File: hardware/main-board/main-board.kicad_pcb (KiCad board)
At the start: 2 copper layers, 180 x 55 mm, 96 parts, among them J1 BARREL_JACK, J2 CONN_01X10, J3 CONN_01X10, J4 USB_OTG, J5 CONN_02X05, J6 SMA, Q1 DDTD113ZC, Q2 DDTD113ZC, Q3 DDTD113ZC, Q4 DDTD113ZC, Q5 DDTD113ZC, Q6 FDB14N30TM, Q7 DDTD113ZC, Q8 DDTD113ZC, Q9 DDTD113ZC, SW1 SW_Push, SW2 SW_Push, SW3 SW_Push, SW4 SW_Push, U1 LD1117S33TR, U2 MAX1771, U3 STM32F302C, U4 FGPMMOPA6H, Y1 8MHz, Y2 32.768kHz

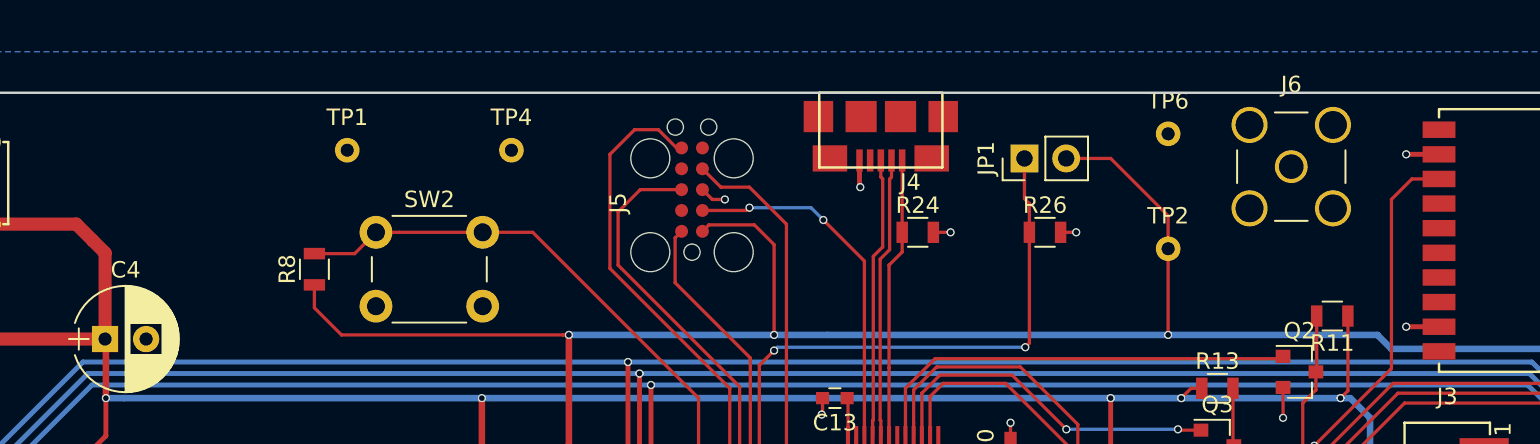
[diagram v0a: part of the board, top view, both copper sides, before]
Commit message: Working on main board layout
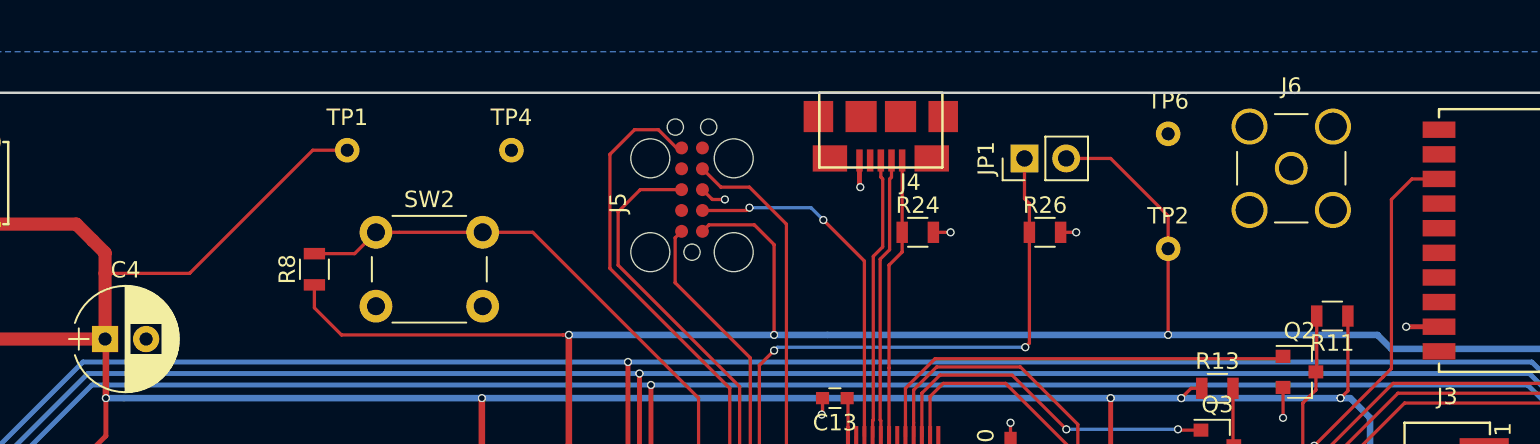
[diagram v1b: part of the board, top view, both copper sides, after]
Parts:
- moved J6 0.10 mm to (202.5, 67.1)
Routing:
- net +12V: track 323.1 -> 340.9 mm
- net GND: track 90.2 -> 88.2 mm, vias 56 -> 55
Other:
- rule trace_min: 0.2 -> 0.16
- rule via_min_drill: 0.34 -> 0.3
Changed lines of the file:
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@@
   (general
     (links 231)
-    (no_connects 14)
+    (no_connects 7)
     (area 59.924999 62.424999 240.075001 117.575001)
     (thickness 1.6)
     (drawings 28)
-    (tracks 898)
+    (tracks 900)
     (zones 0)
     (modules 96)
@@
   )
   (setup
-    (last_trace_width 0.3)
+    (last_trace_width 0.2)
     (user_trace_width 0.3)
     (user_trace_width 0.4)
@@
     (zone_clearance 0.5)
     (zone_45_only no)
-    (trace_min 0.2)
+    (trace_min 0.16)
     (segment_width 0.15)
     (edge_width 0.15)
@@
     (via_drill 0.34)
     (via_min_size 0.5)
-    (via_min_drill 0.34)
+    (via_min_drill 0.3)
     (user_via 0.7 0.5)
     (uvia_size 0.5)
@@
     (uvias_allowed no)
     (uvia_min_size 0.5)
-    (uvia_min_drill 0.34)
+    (uvia_min_drill 0.3)
     (pcb_text_width 0.3)
     (pcb_text_size 1.5 1.5)
@@
   )
   (module Connect:SMA_THT_Jack_Straight (layer F.Cu)
-    (at 202.5 67)
+    (at 202.5 67.1)
     (descr "SMA pcb through hole jack")
     (tags "SMA THT Jack Straight")
@@
       (effects (font (size 1 1) (thickness 0.15)))
     )
-    (fp_text value MountingHole_3.2mm_M3_Pad (at 0 4.2) (layer F.Fab)
+    (fp_text value MountingHole_3.2mm_M3_Pad (at 0 4.2) (layer F.Fab) hide
       (effects (font (size 1 1) (thickness 0.15)))
     )
@@
       (effects (font (size 1 1) (thickness 0.15)))
     )
-    (fp_text value MountingHole_3.2mm_M3_Pad (at 0 4.2) (layer F.Fab)
+    (fp_text value MountingHole_3.2mm_M3_Pad (at 0 4.2) (layer F.Fab) hide
       (effects (font (size 1 1) (thickness 0.15)))
     )
@@
       (effects (font (size 1 1) (thickness 0.15)))
     )
-    (fp_text value MountingHole_3.2mm_M3_Pad (at 0 4.2) (layer F.Fab)
+    (fp_text value MountingHole_3.2mm_M3_Pad (at 0 4.2) (layer F.Fab) hide
       (effects (font (size 1 1) (thickness 0.15)))
     )
@@
       (effects (font (size 1 1) (thickness 0.15)))
     )
-    (fp_text value MountingHole_3.2mm_M3_Pad (at 0 4.2) (layer F.Fab)
+    (fp_text value MountingHole_3.2mm_M3_Pad (at 0 4.2) (layer F.Fab) hide
       (effects (font (size 1 1) (thickness 0.15)))
     )
@@
   (segment (start 83.305 85.555) (end 83.25 85.5) (width 0.6) (layer F.Cu) (net 1))
   (via (at 83.25 85.5) (size 0.7) (drill 0.5) (layers F.Cu B.Cu) (net 1))
-  (segment (start 211.5 66.25) (end 209.5 66.25) (width 0.3) (layer F.Cu) (net 1))
-  (via (at 209.5 66.25) (size 0.5) (drill 0.34) (layers F.Cu B.Cu) (net 1))
   (segment (start 211.5 76.75) (end 209.5 76.75) (width 0.3) (layer F.Cu) (net 1))
   (via (at 209.5 76.75) (size 0.5) (drill 0.34) (layers F.Cu B.Cu) (net 1))
@@
   (via (at 174.6 96) (size 0.5) (drill 0.34) (layers F.Cu B.Cu) (net 2))
   (segment (start 206.5 107.5) (end 211.8 107.5) (width 0.2) (layer F.Cu) (net 2))
+  (segment (start 145 66) (end 142.9 66) (width 0.2) (layer F.Cu) (net 3))
+  (segment (start 142.9 66) (end 135.4 73.5) (width 0.2) (layer F.Cu) (net 3))
+  (segment (start 135.4 73.5) (end 130.25 73.5) (width 0.2) (layer F.Cu) (net 3))
+  (segment (start 130.25 77.5) (end 130.25 73.5) (width 0.8) (layer F.Cu) (net 3))
+  (segment (start 130.25 73.5) (end 130.25 72.25) (width 0.8) (layer F.Cu) (net 3))
   (segment (start 67.55 90) (end 67.55 93) (width 0.3) (layer F.Cu) (net 3))
   (segment (start 67.55 87) (end 67.55 90) (width 0.3) (layer F.Cu) (net 3))
@@
   (via (at 65.75 87) (size 0.7) (drill 0.5) (layers F.Cu B.Cu) (net 3))
   (segment (start 119.5 77.5) (end 130.25 77.5) (width 0.8) (layer F.Cu) (net 3))
-  (segment (start 130.25 77.5) (end 130.25 72.25) (width 0.8) (layer F.Cu) (net 3))
   (segment (start 128.5 70.5) (end 123.1 70.5) (width 0.8) (layer F.Cu) (net 3))
   (segment (start 123.1 65.5) (end 123.1 70.5) (width 0.8) (layer F.Cu) (net 3))

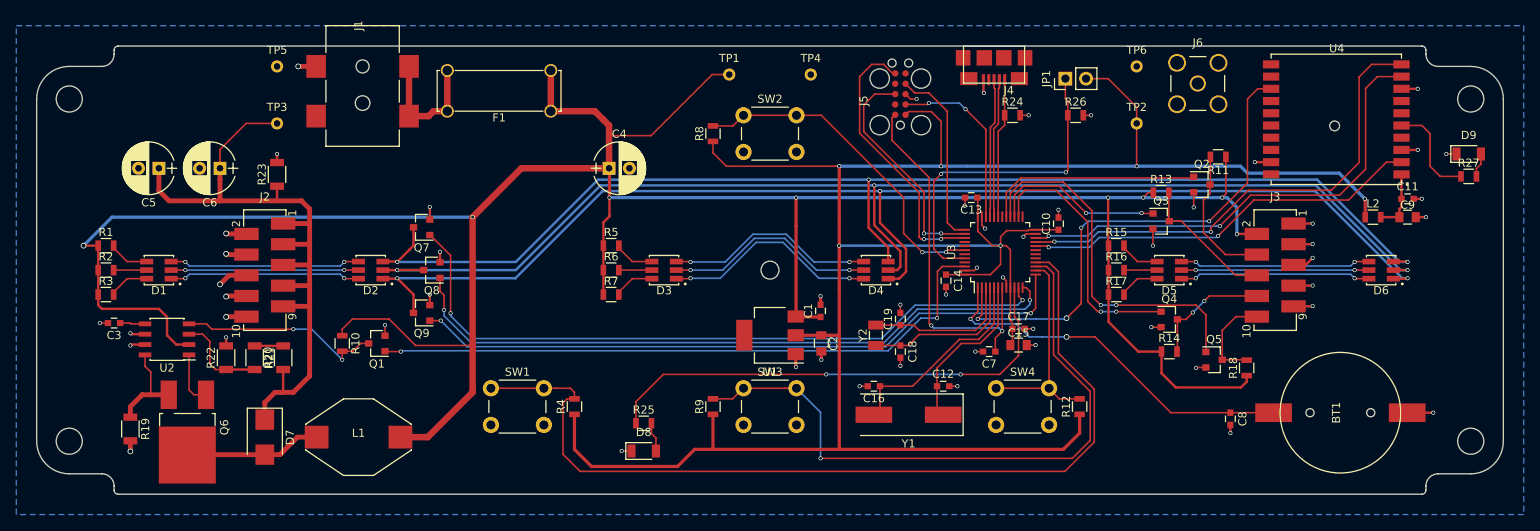
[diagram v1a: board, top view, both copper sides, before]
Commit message: Working on main board layout
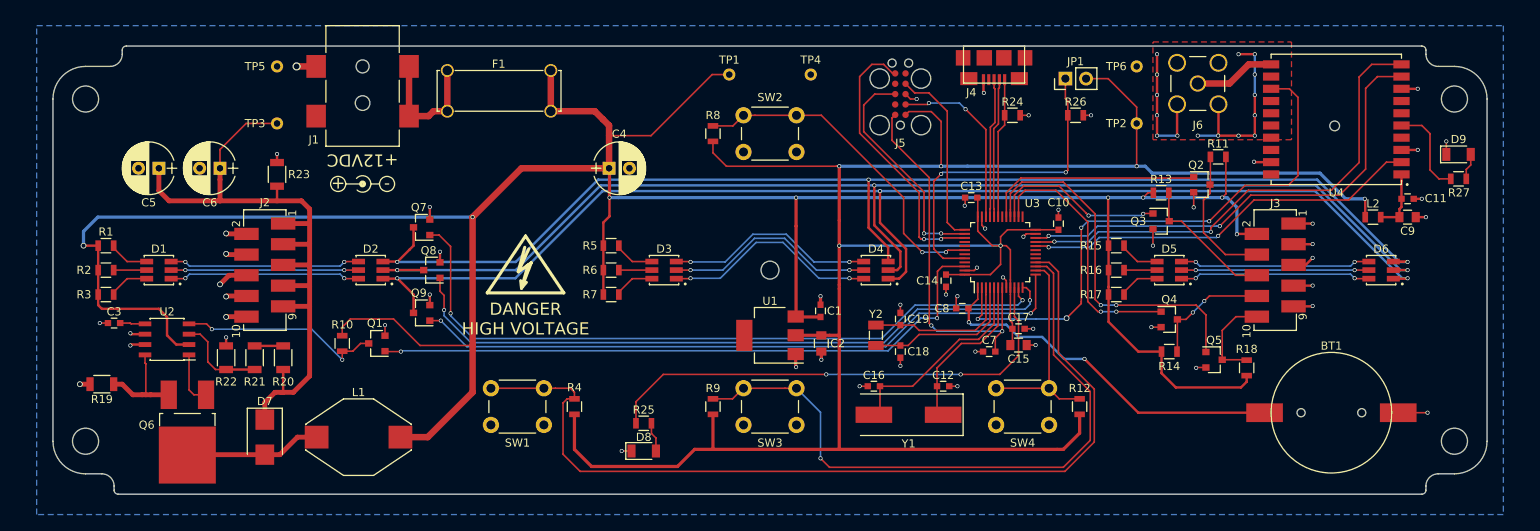
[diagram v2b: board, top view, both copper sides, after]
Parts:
- added REF**: Symbol_HighVoltage_Type2_CopperTop_VerySmall, radio-clock:Symbol_HighVoltage_Type2_SilkscreenTop_VerySmall, F.Cu at (120.0, 90.0)
- added REF**: Symbol_Barrel_Polarity, Symbols:Symbol_Barrel_Polarity, F.Cu at (100.0, 79.5)
- moved C8 35.6 mm to (173.6, 94.7), turned to 180 degrees
- moved R19 6.52 mm to (68.0, 104.0), turned to 180 degrees
- moved REF** 2.00 mm to (66.0, 69.0)
- moved REF** 2.00 mm to (66.0, 111.0)
- moved REF** 2.00 mm to (234.0, 69.0)
- moved REF** 2.00 mm to (234.0, 111.0)
- moved R27 1.29 mm to (234.5, 78.8)
- moved D9 1.25 mm to (234.5, 75.8)
- moved BT1 1.10 mm to (218.9, 107.5)
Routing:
- net GND: track 88.2 -> 129.0 mm, vias 55 -> 70
- net Net-(J6-Pad1): track 0.00 -> 9.97 mm
- net /GPS_PPS: track 63.2 -> 69.4 mm
- net +12V: track 340.9 -> 342.1 mm
- net /PB2: track 79.5 -> 80.4 mm
- net Net-(R27-Pad1): track 12.2 -> 11.4 mm
- net /LED_RED: track 86.0 -> 86.7 mm
- net Net-(BT1-Pad1): track 46.2 -> 45.7 mm
- added copper zone on F.Cu, net GND
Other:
- board size 180 x 55 mm -> 176 x 55 mm
- board text added: "+"
- board text added: "+12VDC"
- board text added: "-"
- board text added: "DANGER HIGH VOLTAGE"

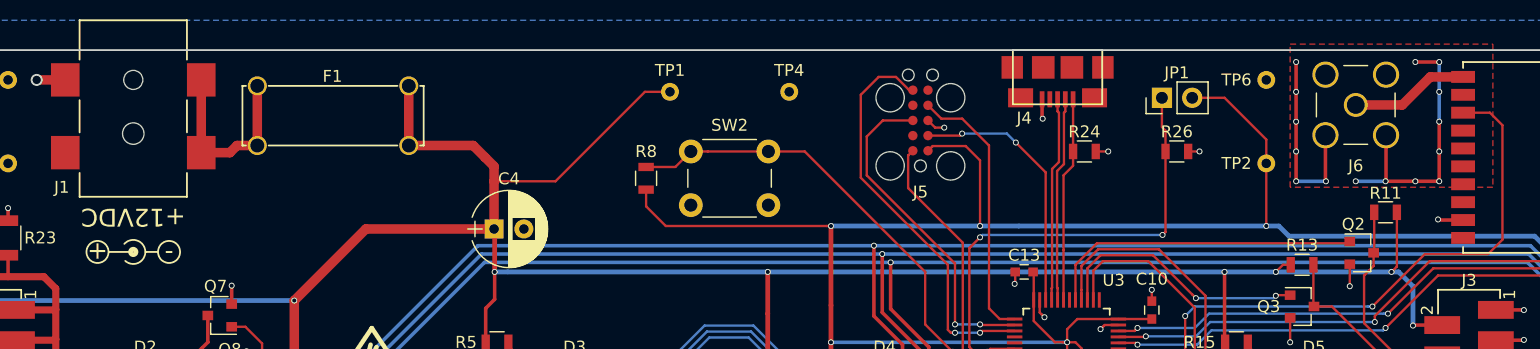
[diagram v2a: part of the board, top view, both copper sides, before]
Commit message: Working on main board layout
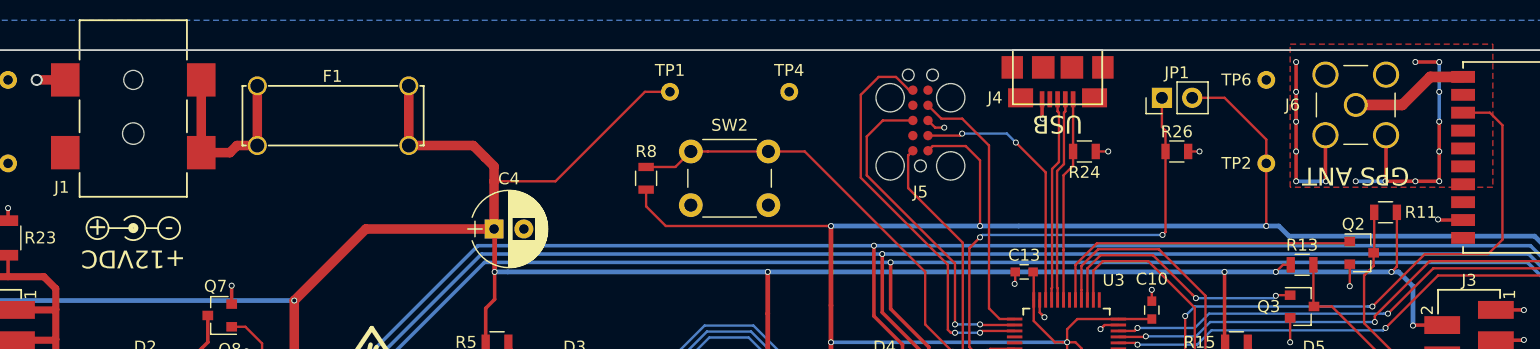
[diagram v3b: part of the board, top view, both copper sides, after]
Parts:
- moved REF** 2.00 mm to (100.0, 77.5)
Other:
- board text added: "GPS ANT"
- board text added: "USB"
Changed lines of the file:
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@@
     (area 61.924999 62.424999 238.075001 117.575001)
     (thickness 1.6)
-    (drawings 32)
+    (drawings 34)
     (tracks 942)
     (zones 0)
@@
   (module radio-clock:10118192 (layer F.Cu)
     (at 177.5 62.5 180)
-    (fp_text reference J4 (at 2.8 -5.7 180) (layer F.SilkS)
+    (fp_text reference J4 (at 5.25 -4 180) (layer F.SilkS)
       (effects (font (size 1 1) (thickness 0.15)))
     )
@@
     (descr "SMA pcb through hole jack")
     (tags "SMA THT Jack Straight")
-    (fp_text reference J6 (at 0 5.1) (layer F.SilkS)
+    (fp_text reference J6 (at -5.3 0) (layer F.SilkS)
       (effects (font (size 1 1) (thickness 0.15)))
     )
@@
     (tags "resistor 0805")
     (attr smd)
-    (fp_text reference R11 (at 0 1.6 180) (layer F.SilkS)
+    (fp_text reference R11 (at -2.95 0 180) (layer F.SilkS)
       (effects (font (size 1 1) (thickness 0.15)))
     )
@@
     (tags "resistor 0805")
     (attr smd)
-    (fp_text reference R24 (at 0 -1.65) (layer F.SilkS)
+    (fp_text reference R24 (at 0 1.75) (layer F.SilkS)
       (effects (font (size 1 1) (thickness 0.15)))
     )
@@
   )
   (module Symbols:Symbol_Barrel_Polarity (layer F.Cu)
-    (at 100 79.5 180)
+    (at 100 77.5 180)
     (descr "Barrel connector polarity indicator")
     (tags "barrel polarity")
@@
     (fp_arc (start 0 0.075) (end 0.75 0.75) (angle 270) (layer F.SilkS) (width 0.15))
   )
+  (gr_text USB (at 177.5 68.7 180) (layer F.SilkS)
+    (effects (font (size 1.5 1.5) (thickness 0.3)))
+  )
+  (gr_text "GPS ANT" (at 202.5 73.05 180) (layer F.SilkS)
+    (effects (font (size 1.5 1.5) (thickness 0.3)))
+  )
   (gr_line (start 71 62.5) (end 230 62.5) (layer Edge.Cuts) (width 0.15))
   (gr_line (start 230 117.5) (end 70 117.5) (layer Edge.Cuts) (width 0.15))
@@
   (gr_line (start 66 115) (end 68 115) (layer Edge.Cuts) (width 0.15))
   (gr_line (start 66 65) (end 69 65) (layer Edge.Cuts) (width 0.15))
-  (gr_text +12VDC (at 100 76.5 180) (layer F.SilkS)
+  (gr_text +12VDC (at 100 80 180) (layer F.SilkS)
     (effects (font (size 1.5 1.5) (thickness 0.3)))
   )
-  (gr_text - (at 103 79.3) (layer F.SilkS)
+  (gr_text - (at 103 77.3) (layer F.SilkS)
     (effects (font (size 1.5 1.5) (thickness 0.3)))
   )
-  (gr_text + (at 97 79.3) (layer F.SilkS)
+  (gr_text + (at 97 77.3) (layer F.SilkS)
     (effects (font (size 1.5 1.5) (thickness 0.3)))
   )
@@
   (segment (start 162.85 68.4) (end 165.365 68.4) (width 0.2) (layer F.Cu) (net 53))
   (via (at 168.9 85.5) (size 0.5) (drill 0.34) (layers F.Cu B.Cu) (net 53))
-  (segment (start 202.5 67.1) (end 206.4 67.1) (width 0.8) (layer F.Cu) (net 55))
-  (segment (start 206.4 67.1) (end 208.75 64.75) (width 0.8) (layer F.Cu) (net 55))
-  (segment (start 208.75 64.75) (end 211.5 64.75) (width 0.8) (layer F.Cu) (net 55))
+  (segment (start 202.5 67.1) (end 206.4 67.1) (width 0.9) (layer F.Cu) (net 55))
+  (segment (start 206.4 67.1) (end 208.75 64.75) (width 0.9) (layer F.Cu) (net 55))
+  (segment (start 208.75 64.75) (end 211.5 64.75) (width 0.9) (layer F.Cu) (net 55))
   (segment (start 170.1 87.4) (end 170.1 79.1) (width 0.2) (layer F.Cu) (net 56))
   (segment (start 170.1 79.1) (end 170.2 79) (width 0.2) (layer F.Cu) (net 56))

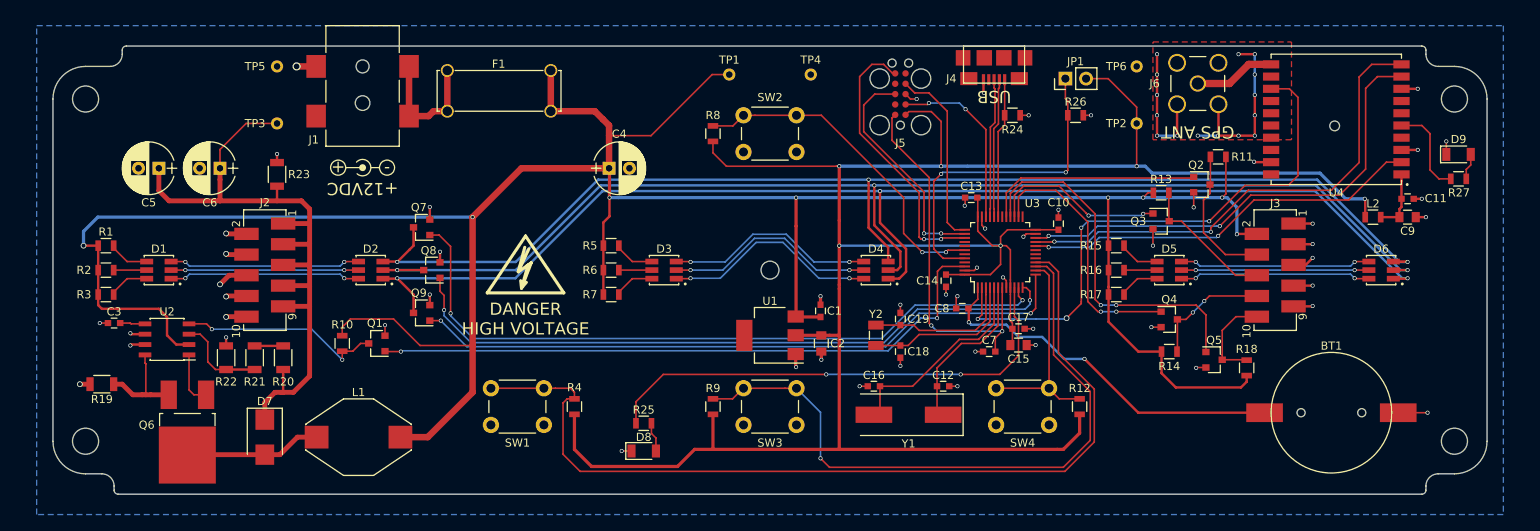
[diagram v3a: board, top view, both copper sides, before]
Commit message: Added bypass cap to MAX1771.  Cleaning up PCB design
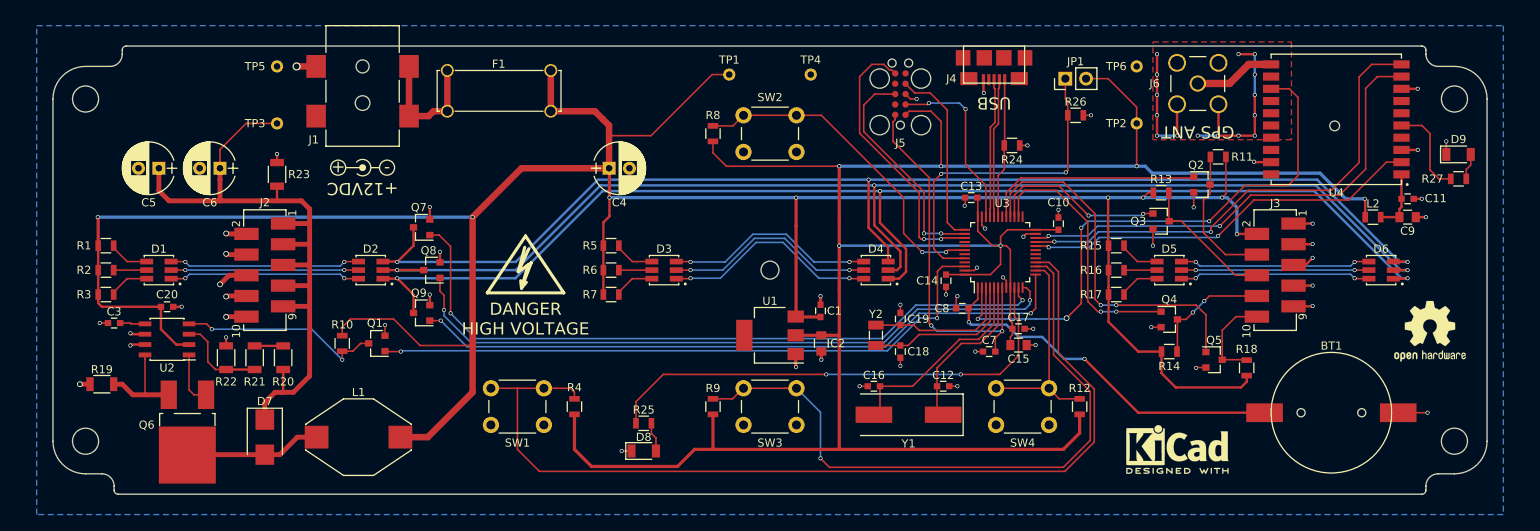
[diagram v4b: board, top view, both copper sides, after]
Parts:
- added C20: 0.1u, Capacitors_SMD:C_0603, F.Cu at (76.0, 94.5)
- added REF***: KiCad-Logo2_6mm_SilkScreen, Symbols:KiCad-Logo2_6mm_SilkScreen, F.Cu at (200.0, 112.0)
- added REF***: OSHW-Logo2_9.8x8mm_SilkScreen, Symbols:OSHW-Logo2_9.8x8mm_SilkScreen, F.Cu at (231.0, 97.5)
- moved R24 3.70 mm to (179.7, 74.7)
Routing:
- net /PB1: track 112.7 -> 118.2 mm
- net +12V: track 342.1 -> 339.7 mm
- net GND: track 129.0 -> 130.0 mm, vias 70 -> 71
